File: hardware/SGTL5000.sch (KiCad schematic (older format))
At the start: 24 parts, among them J2 AudioJack3_Ground, J3 AudioJack3_Ground, U2 MCP1811A, U7 SGTL5000

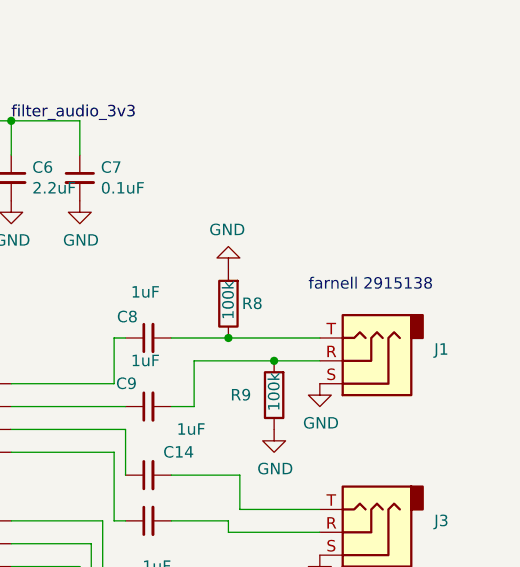
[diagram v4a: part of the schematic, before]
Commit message: change farnell field to farnell #
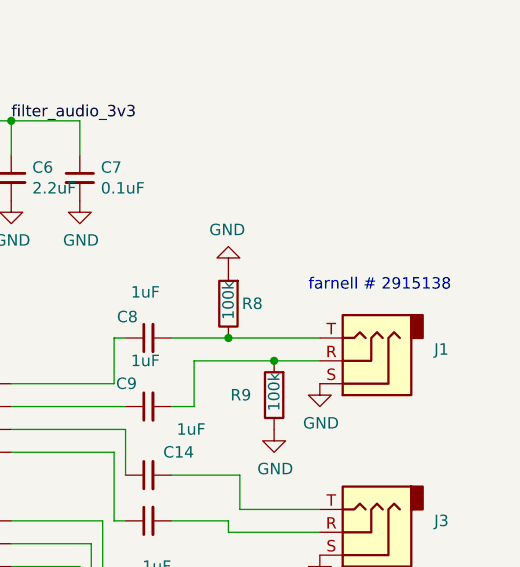
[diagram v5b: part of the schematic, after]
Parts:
- C13, C2, C27, C28, C30: farnell 1414663 -> (none); farnell # (none) -> 1414663
- C14, C15, C8, C9: farnell 2112915 -> (none); farnell # (none) -> 2112915
- C17, C26, C29, C31: farnell 2773238 -> (none); farnell # (none) -> 2773238
- J2, J3: farnell 2915138 -> (none); farnell # (none) -> 2915138
- L2: farnell 2215655 -> (none); farnell # (none) -> 2215655
- R22, R23: farnell 1469887 -> (none); farnell # (none) -> 1469887
- R3: farnell 1469862 -> (none); farnell # (none) -> 1469862
- R8, R9: farnell 1469860 -> (none); farnell # (none) -> 1469860
- U2: farnell 2990195 -> (none); farnell # (none) -> 2990195
- U7: farnell 2308049 -> (none); farnell # (none) -> 2308049
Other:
- note added: "farnell # 2915138"
- note removed: "farnell 2915138"
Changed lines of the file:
@@
 F 1 "AudioJack3_Ground" H 7500 3100 50  0001 R CNN
 F 2 "audio-fx:Jack_3.5mm_CUI_SJ-3523-SMT_Horizontal" H 7900 3050 50  0001 C CNN
-F 3 "https://uk.farnell.com/switchcraft-conxall/35rasmt2bhntrx/connector-smt-3-5mm-ph-jk-tap/dp/2915138" H 7900 3050 50  0001 C CNN
-F 4 "2915138" H 7900 3050 50  0001 C CNN "farnell"
+F 3 "https://uk.farnell #.com/switchcraft-conxall/35rasmt2bhntrx/connector-smt-3-5mm-ph-jk-tap/dp/2915138" H 7900 3050 50  0001 C CNN
+F 4 "2915138" H 7900 3050 50  0001 C CNN "farnell #"
 	1    7900 3050
 	-1   0    0    1
@@
 F 2 "Capacitor_SMD:C_0805_2012Metric" H 4550 2250 50  0001 C CNN
 F 3 "~" H 4550 2250 50  0001 C CNN
-F 4 "2773238" H 4550 2250 50  0001 C CNN "farnell"
+F 4 "2773238" H 4550 2250 50  0001 C CNN "farnell #"
 	1    4550 2250
 	1    0    0    -1
@@
 F 2 "Capacitor_SMD:C_0805_2012Metric" H 4850 2250 50  0001 C CNN
 F 3 "~" H 4850 2250 50  0001 C CNN
-F 4 "1414663" H 4850 2250 50  0001 C CNN "farnell"
+F 4 "1414663" H 4850 2250 50  0001 C CNN "farnell #"
 	1    4850 2250
 	1    0    0    -1
@@
 F 2 "Capacitor_SMD:C_0805_2012Metric" H 5150 2250 50  0001 C CNN
 F 3 "~" H 5150 2250 50  0001 C CNN
-F 4 "1414663" H 5150 2250 50  0001 C CNN "farnell"
+F 4 "1414663" H 5150 2250 50  0001 C CNN "farnell #"
 	1    5150 2250
 	1    0    0    -1
@@
 F 2 "Capacitor_SMD:C_0805_2012Metric" H 6350 2250 50  0001 C CNN
 F 3 "~" H 6350 2250 50  0001 C CNN
-F 4 "2773238" H 6350 2250 50  0001 C CNN "farnell"
+F 4 "2773238" H 6350 2250 50  0001 C CNN "farnell #"
 	1    6350 2250
 	1    0    0    -1
@@
 F 2 "Capacitor_SMD:C_0805_2012Metric" H 6650 2250 50  0001 C CNN
 F 3 "~" H 6650 2250 50  0001 C CNN
-F 4 "1414663" H 6650 2250 50  0001 C CNN "farnell"
+F 4 "1414663" H 6650 2250 50  0001 C CNN "farnell #"
 	1    6650 2250
 	1    0    0    -1
@@
 F 2 "Inductor_SMD:L_0805_2012Metric" V 5780 2000 50  0001 C CNN
 F 3 "~" H 5850 2000 50  0001 C CNN
-F 4 "2215655" H 5850 2000 50  0001 C CNN "farnell"
+F 4 "2215655" H 5850 2000 50  0001 C CNN "farnell #"
 	1    5850 2000
 	0    -1   -1   0
@@
 F 2 "Resistor_SMD:R_0805_2012Metric" V 4530 2950 50  0001 C CNN
 F 3 "~" H 4600 2950 50  0001 C CNN
-F 4 "1469887" H 4600 2950 50  0001 C CNN "farnell"
+F 4 "1469887" H 4600 2950 50  0001 C CNN "farnell #"
 	1    4600 2950
 	1    0    0    -1
@@
 F 2 "Resistor_SMD:R_0805_2012Metric" V 4830 2950 50  0001 C CNN
 F 3 "~" H 4900 2950 50  0001 C CNN
-F 4 "1469887" H 4900 2950 50  0001 C CNN "farnell"
+F 4 "1469887" H 4900 2950 50  0001 C CNN "farnell #"
 	1    4900 2950
 	1    0    0    -1
@@
 F 2 "audio-fx:Jack_3.5mm_CUI_SJ-3523-SMT_Horizontal" H 7900 4200 50  0001 C CNN
 F 3 "~" H 7900 4200 50  0001 C CNN
-F 4 "2915138" H 7900 4200 50  0001 C CNN "farnell"
+F 4 "2915138" H 7900 4200 50  0001 C CNN "farnell #"
 	1    7900 4200
 	-1   0    0    1
@@
 F 2 "Capacitor_SMD:C_0805_2012Metric" H 4450 4200 50  0001 C CNN
 F 3 "~" H 4450 4200 50  0001 C CNN
-F 4 "1414663" H 4450 4200 50  0001 C CNN "farnell"
+F 4 "1414663" H 4450 4200 50  0001 C CNN "farnell #"
 	1    4450 4200
 	1    0    0    -1
@@
 F 2 "Package_DFN_QFN:QFN-32-1EP_5x5mm_P0.5mm_EP3.6x3.6mm" H 5650 3800 60  0001 C CNN
 F 3 "https://www.nxp.com/docs/en/data-sheet/SGTL5000.pdf" H 5600 2100 60  0000 C CNN
-F 4 "2308049" H 5650 3750 50  0001 C CNN "farnell"
+F 4 "2308049" H 5650 3750 50  0001 C CNN "farnell #"
 	1    5650 3750
 	1    0    0    -1
@@
 F 1 "1uF" V 7150 2900 50  0000 L CNN
 F 2 "Capacitor_SMD:C_1210_3225Metric" H 6950 2950 50  0001 C CNN
-F 3 "http://www.farnell.com/datasheets/199119.pdf" H 6950 2950 50  0001 C CNN
-F 4 "2112915" V 6950 2950 50  0001 C CNN "farnell"
+F 3 "http://www.farnell #.com/datasheets/199119.pdf" H 6950 2950 50  0001 C CNN
+F 4 "2112915" V 6950 2950 50  0001 C CNN "farnell #"
 	1    6950 2950
 	0    -1   -1   0
@@
 F 2 "Capacitor_SMD:C_1210_3225Metric" H 6950 3250 50  0001 C CNN
 F 3 "~" H 6950 3250 50  0001 C CNN
-F 4 "2112915" H 6950 3250 50  0001 C CNN "farnell"
+F 4 "2112915" H 6950 3250 50  0001 C CNN "farnell #"
 	1    6950 3250
 	0    -1   -1   0
@@
 	7050 3250 7150 3250
 Text Notes 7650 2750 0    50   ~ 0
-farnell 2915138
+farnell # 2915138
 $Comp
 L Device:R R?
@@
 F 2 "Resistor_SMD:R_0805_2012Metric" V 4430 3450 50  0001 C CNN
 F 3 "~" H 4500 3450 50  0001 C CNN
-F 4 "1469862" H 4500 3450 50  0001 C CNN "farnell"
+F 4 "1469862" H 4500 3450 50  0001 C CNN "farnell #"
 	1    4500 3450
 	0    1    1    0
@@
 F 2 "Capacitor_SMD:C_0805_2012Metric" H 6550 4250 50  0001 C CNN
 F 3 "~" H 6550 4250 50  0001 C CNN
-F 4 "1414663" H 6550 4250 50  0001 C CNN "farnell"
+F 4 "1414663" H 6550 4250 50  0001 C CNN "farnell #"
 	1    6550 4250
 	1    0    0    -1
@@
 F 2 "Resistor_SMD:R_0805_2012Metric" V 7230 2800 50  0001 C CNN
 F 3 "~" H 7300 2800 50  0001 C CNN
-F 4 "1469860" H 7300 2800 50  0001 C CNN "farnell"
+F 4 "1469860" H 7300 2800 50  0001 C CNN "farnell #"
 	1    7300 2800
 	-1   0    0    1
@@
 F 2 "Resistor_SMD:R_0805_2012Metric" V 7430 3200 50  0001 C CNN
 F 3 "~" H 7500 3200 50  0001 C CNN
-F 4 "1469860" H 7500 3200 50  0001 C CNN "farnell"
+F 4 "1469860" H 7500 3200 50  0001 C CNN "farnell #"
 	1    7500 3200
 	-1   0    0    1
@@
 F 2 "audio-fx:Jack_3.5mm_CUI_SJ-3523-SMT_Horizontal" H 7900 3800 50  0001 C CNN
 F 3 "~" H 7900 3800 50  0001 C CNN
-F 4 "2915138" H 7900 3800 50  0001 C CNN "farnell"
+F 4 "2915138" H 7900 3800 50  0001 C CNN "farnell #"
 	1    7900 3800
 	-1   0    0    1
@@
 F 2 "Capacitor_SMD:C_1210_3225Metric" H 6950 3550 50  0001 C CNN
 F 3 "~" H 6950 3550 50  0001 C CNN
-F 4 "2112915" H 6950 3550 50  0001 C CNN "farnell"
+F 4 "2112915" H 6950 3550 50  0001 C CNN "farnell #"
 	1    6950 3550
 	0    -1   -1   0
@@
 F 2 "Capacitor_SMD:C_1210_3225Metric" H 6950 3750 50  0001 C CNN
 F 3 "~" H 6950 3750 50  0001 C CNN
-F 4 "2112915" H 6950 3750 50  0001 C CNN "farnell"
+F 4 "2112915" H 6950 3750 50  0001 C CNN "farnell #"
 	1    6950 3750
 	0    -1   -1   0
@@
 F 2 "Capacitor_SMD:C_0805_2012Metric" H 2750 2200 50  0001 C CNN
 F 3 "~" H 2750 2200 50  0001 C CNN
-F 4 "2773238" H 2750 2200 50  0001 C CNN "farnell"
+F 4 "2773238" H 2750 2200 50  0001 C CNN "farnell #"
 	1    2750 2200
 	1    0    0    -1
@@
 F 1 "MCP1811A" H 2150 2274 50  0000 C CNN
 F 2 "Package_TO_SOT_SMD:SOT-23" H 2150 2100 50  0001 C CNN
-F 3 "http://www.farnell.com/datasheets/2722379.pdf" H 2150 2100 50  0001 C CNN
-F 4 "2990195" H 2150 2100 50  0001 C CNN "farnell"
+F 3 "http://www.farnell #.com/datasheets/2722379.pdf" H 2150 2100 50  0001 C CNN
+F 4 "2990195" H 2150 2100 50  0001 C CNN "farnell #"
 	1    2150 2100
 	1    0    0    -1
@@
 F 2 "Capacitor_SMD:C_0805_2012Metric" H 1550 2350 50  0001 C CNN
 F 3 "~" H 1550 2350 50  0001 C CNN
-F 4 "2773238" H 1550 2350 50  0001 C CNN "farnell"
+F 4 "2773238" H 1550 2350 50  0001 C CNN "farnell #"
 	1    1550 2350
 	1    0    0    -1

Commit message: fix library mess and get bom exported
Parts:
- U2: symbol teensy-fx-rescue:ldo -> teensy-fx:ldo
- U7: symbol teensy-fx-rescue:SparkFun-IC-Analog_SGTL5000-teensy_beats-cache -> teensy-fx:SparkFun-IC-Analog_SGTL5000-teensy_beats-cache
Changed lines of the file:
@@
 NoConn ~ 6350 4300
 $Comp
-L teensy-fx-rescue:SparkFun-IC-Analog_SGTL5000-teensy_beats-cache U?
+L teensy-fx:SparkFun-IC-Analog_SGTL5000-teensy_beats-cache U?
 U 1 1 5BAC3E38
 P 5650 3750
@@
 $EndComp
 $Comp
-L teensy-fx-rescue:ldo U2
+L teensy-fx:ldo U2
 U 1 1 5E1AE9E1
 P 2150 2100

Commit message: cheaper caps and non-us 10k resistor
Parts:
- C17, C26, C29, C31: farnell # 2773238 -> 1759424
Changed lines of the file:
@@
 F 2 "Capacitor_SMD:C_0805_2012Metric" H 4550 2250 50  0001 C CNN
 F 3 "~" H 4550 2250 50  0001 C CNN
-F 4 "2773238" H 4550 2250 50  0001 C CNN "farnell #"
+F 4 "1759424" H 4550 2250 50  0001 C CNN "farnell #"
 	1    4550 2250
 	1    0    0    -1
@@
 F 2 "Capacitor_SMD:C_0805_2012Metric" H 6350 2250 50  0001 C CNN
 F 3 "~" H 6350 2250 50  0001 C CNN
-F 4 "2773238" H 6350 2250 50  0001 C CNN "farnell #"
+F 4 "1759424" H 6350 2250 50  0001 C CNN "farnell #"
 	1    6350 2250
 	1    0    0    -1
@@
 F 2 "Capacitor_SMD:C_0805_2012Metric" H 2750 2200 50  0001 C CNN
 F 3 "~" H 2750 2200 50  0001 C CNN
-F 4 "2773238" H 2750 2200 50  0001 C CNN "farnell #"
+F 4 "1759424" H 2750 2200 50  0001 C CNN "farnell #"
 	1    2750 2200
 	1    0    0    -1
@@
 F 2 "Capacitor_SMD:C_0805_2012Metric" H 1550 2350 50  0001 C CNN
 F 3 "~" H 1550 2350 50  0001 C CNN
-F 4 "2773238" H 1550 2350 50  0001 C CNN "farnell #"
+F 4 "1759424" H 1550 2350 50  0001 C CNN "farnell #"
 	1    1550 2350
 	1    0    0    -1
